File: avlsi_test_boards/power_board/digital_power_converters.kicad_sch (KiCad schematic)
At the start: 21 parts, among them U1 TLV1117LV18DCYR, U15 DS04-254-2-04BK-SMT, U20 74HC4051D_653, U3 TLV1117LV25DCYR, U4 TLV1117LV33DCYR

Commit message: Fully routed
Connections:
- net AVIN renamed VDCustom
- net GND renamed DGND
- net VIN renamed DVIN5

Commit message: Add partial changes
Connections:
- net NULL is gone; now on net DGND: U20.2 (Y6), U20.4 (Y7)
- net DGND: now also U15.5
- net VCCD12: now also U20.14 (Y1); no longer U20.15 (Y2)
- net VCCD18: now also U20.15 (Y2); no longer U20.14 (Y1)
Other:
- moved on the sheet: C18, R15, R16, R17

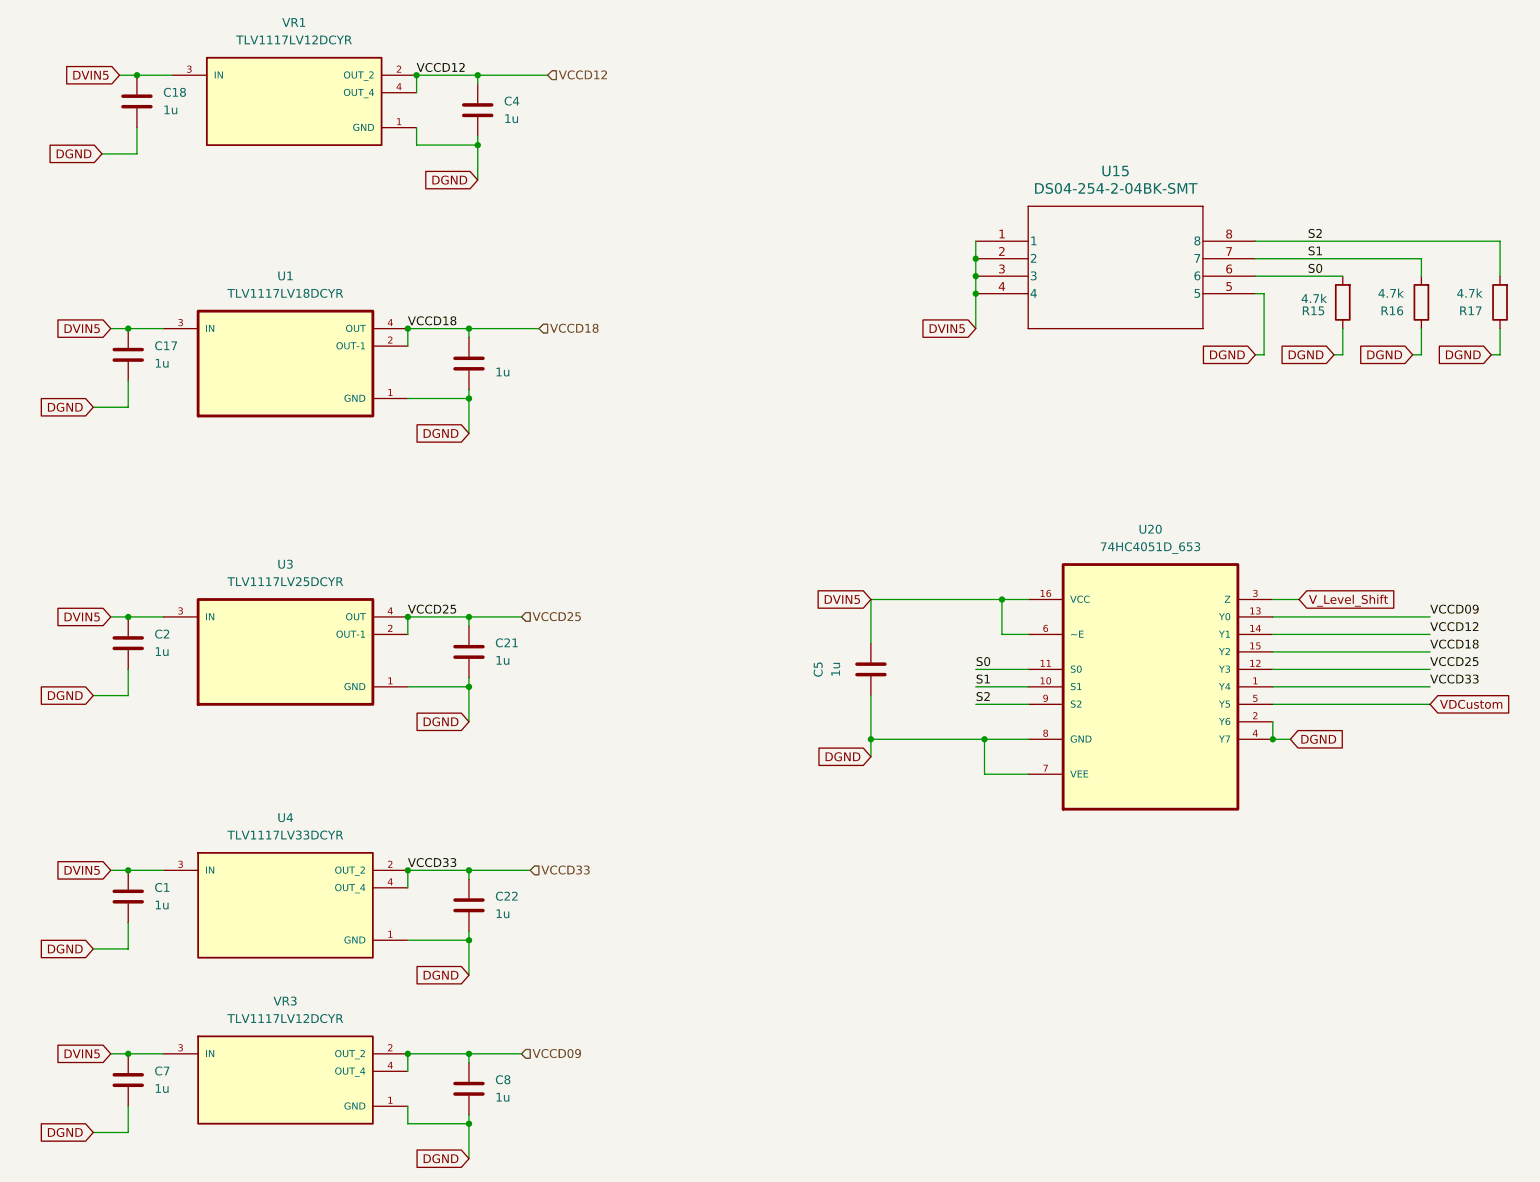
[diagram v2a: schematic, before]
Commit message: Add updated schematic
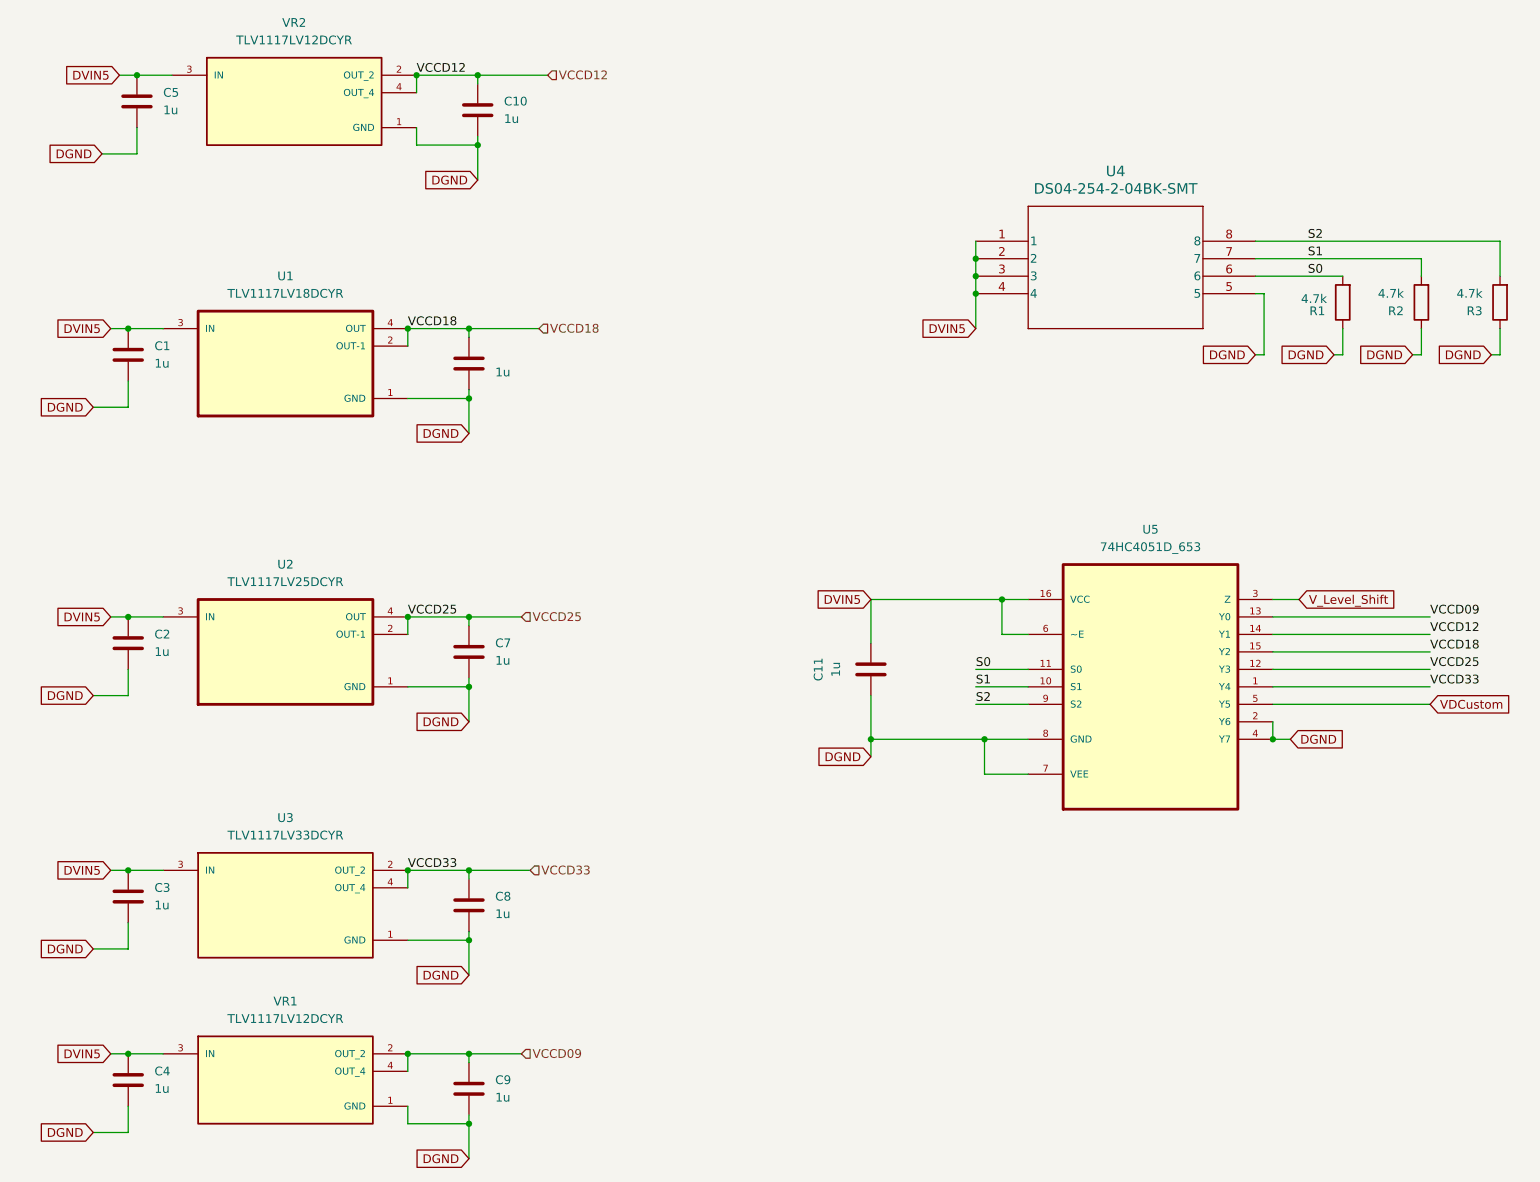
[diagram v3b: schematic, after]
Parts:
- renumbered C17 to C1, C4 to C10, C5 to C11, C1 to C3, C7 to C4, C18 to C5, C3 to C6, C21 to C7, C22 to C8, C8 to C9, R15 to R1, R16 to R2, R17 to R3, U3 to U2, U4 to U3, U15 to U4, U20 to U5, VR3 to VR1, VR1 to VR2
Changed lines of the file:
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@@
 		(dnp no)
 		(fields_autoplaced yes)
-		(property "Reference" "C18"
+		(property "Reference" "C5"
 			(at 64.77 40.6399 0)
 			(effects
@@
 			(project "power_board"
 				(path "/425e3f4e-d960-41c8-a4b7-4f888de39c97/572e1625-24a1-4783-bac1-8c305a89efd3"
-					(reference "C18")
+					(reference "C5")
 					(unit 1)
 				)
@@
 		(on_board yes)
 		(dnp no)
-		(property "Reference" "C5"
+		(property "Reference" "C11"
 			(at 160.02 124.46 90)
 			(effects
@@
 			(project "power_board"
 				(path "/425e3f4e-d960-41c8-a4b7-4f888de39c97/572e1625-24a1-4783-bac1-8c305a89efd3"
-					(reference "C5")
+					(reference "C11")
 					(unit 1)
 				)
@@
 		(dnp no)
 		(fields_autoplaced yes)
-		(property "Reference" "VR1"
+		(property "Reference" "VR2"
 			(at 83.82 30.48 0)
 			(effects
@@
 			(project "power_board"
 				(path "/425e3f4e-d960-41c8-a4b7-4f888de39c97/572e1625-24a1-4783-bac1-8c305a89efd3"
-					(reference "VR1")
+					(reference "VR2")
 					(unit 1)
 				)
@@
 		(dnp no)
 		(fields_autoplaced yes)
-		(property "Reference" "C21"
+		(property "Reference" "C7"
 			(at 113.03 120.6499 0)
 			(effects
@@
 			(project "power_board"
 				(path "/425e3f4e-d960-41c8-a4b7-4f888de39c97/572e1625-24a1-4783-bac1-8c305a89efd3"
-					(reference "C21")
+					(reference "C7")
 					(unit 1)
 				)
@@
 		(dnp no)
 		(fields_autoplaced yes)
-		(property "Reference" "C4"
+		(property "Reference" "C10"
 			(at 114.3 41.9099 0)
 			(effects
@@
 			(project "power_board"
 				(path "/425e3f4e-d960-41c8-a4b7-4f888de39c97/572e1625-24a1-4783-bac1-8c305a89efd3"
-					(reference "C4")
+					(reference "C10")
 					(unit 1)
 				)
@@
 		(dnp no)
 		(fields_autoplaced yes)
-		(property "Reference" "C7"
+		(property "Reference" "C4"
 			(at 63.5 182.8799 0)
 			(effects
@@
 			(project "power_board"
 				(path "/425e3f4e-d960-41c8-a4b7-4f888de39c97/572e1625-24a1-4783-bac1-8c305a89efd3"
-					(reference "C7")
+					(reference "C4")
 					(unit 1)
 				)
@@
 		(dnp no)
 		(fields_autoplaced yes)
-		(property "Reference" "VR3"
+		(property "Reference" "VR1"
 			(at 82.55 172.72 0)
 			(effects
@@
 			(project "power_board"
 				(path "/425e3f4e-d960-41c8-a4b7-4f888de39c97/572e1625-24a1-4783-bac1-8c305a89efd3"
-					(reference "VR3")
+					(reference "VR1")
 					(unit 1)
 				)
@@
 		(dnp no)
 		(fields_autoplaced yes)
-		(property "Reference" "U3"
+		(property "Reference" "U2"
 			(at 82.55 109.22 0)
 			(effects
@@
 			(project "power_board"
 				(path "/425e3f4e-d960-41c8-a4b7-4f888de39c97/572e1625-24a1-4783-bac1-8c305a89efd3"
-					(reference "U3")
+					(reference "U2")
 					(unit 1)
 				)
@@
 		(dnp no)
 		(fields_autoplaced yes)
-		(property "Reference" "C22"
+		(property "Reference" "C8"
 			(at 113.03 157.4799 0)
 			(effects
@@
 			(project "power_board"
 				(path "/425e3f4e-d960-41c8-a4b7-4f888de39c97/572e1625-24a1-4783-bac1-8c305a89efd3"
-					(reference "C22")
+					(reference "C8")
 					(unit 1)
 				)
@@
 		(dnp no)
 		(fields_autoplaced yes)
-		(property "Reference" "C8"
+		(property "Reference" "C9"
 			(at 113.03 184.1499 0)
 			(effects
@@
 			(project "power_board"
 				(path "/425e3f4e-d960-41c8-a4b7-4f888de39c97/572e1625-24a1-4783-bac1-8c305a89efd3"
-					(reference "C8")
+					(reference "C9")
 					(unit 1)
 				)
@@
 		(dnp no)
 		(fields_autoplaced yes)
-		(property "Reference" "C1"
+		(property "Reference" "C3"
 			(at 63.5 156.2099 0)
 			(effects
@@
 			(project "power_board"
 				(path "/425e3f4e-d960-41c8-a4b7-4f888de39c97/572e1625-24a1-4783-bac1-8c305a89efd3"
-					(reference "C1")
+					(reference "C3")
 					(unit 1)
 				)
@@
 		(dnp no)
 		(fields_autoplaced yes)
-		(property "Reference" "C3"
+		(property "Reference" "C6"
 			(at 113.03 78.7399 0)
 			(effects
@@
 			(project "power_board"
 				(path "/425e3f4e-d960-41c8-a4b7-4f888de39c97/572e1625-24a1-4783-bac1-8c305a89efd3"
-					(reference "C3")
+					(reference "C6")
 					(unit 1)
 				)
@@
 		(dnp no)
 		(fields_autoplaced yes)
-		(property "Reference" "R17"
+		(property "Reference" "R3"
 			(at 256.54 72.3901 0)
 			(effects
@@
 			(project "power_board"
 				(path "/425e3f4e-d960-41c8-a4b7-4f888de39c97/572e1625-24a1-4783-bac1-8c305a89efd3"
-					(reference "R17")
+					(reference "R3")
 					(unit 1)
 				)
@@
 		(dnp no)
 		(fields_autoplaced yes)
-		(property "Reference" "U20"
+		(property "Reference" "U5"
 			(at 208.28 104.14 0)
 			(effects
@@
 			(project "power_board"
 				(path "/425e3f4e-d960-41c8-a4b7-4f888de39c97/572e1625-24a1-4783-bac1-8c305a89efd3"
-					(reference "U20")
+					(reference "U5")
 					(unit 1)
 				)
@@
 		(dnp no)
 		(fields_autoplaced yes)
-		(property "Reference" "R16"
+		(property "Reference" "R2"
 			(at 245.11 72.3901 0)
 			(effects
@@
 			(project "power_board"
 				(path "/425e3f4e-d960-41c8-a4b7-4f888de39c97/572e1625-24a1-4783-bac1-8c305a89efd3"
-					(reference "R16")
+					(reference "R2")
 					(unit 1)
 				)
@@
 		(dnp no)
 		(fields_autoplaced yes)
-		(property "Reference" "U15"
+		(property "Reference" "U4"
 			(at 203.2 52.07 0)
 			(effects
@@
 			(project "power_board"
 				(path "/425e3f4e-d960-41c8-a4b7-4f888de39c97/572e1625-24a1-4783-bac1-8c305a89efd3"
-					(reference "U15")
+					(reference "U4")
 					(unit 1)
 				)
@@
 		(dnp no)
 		(fields_autoplaced yes)
-		(property "Reference" "C17"
+		(property "Reference" "C1"
 			(at 63.5 77.4699 0)
 			(effects
@@
 			(project "power_board"
 				(path "/425e3f4e-d960-41c8-a4b7-4f888de39c97/572e1625-24a1-4783-bac1-8c305a89efd3"
-					(reference "C17")
+					(reference "C1")
 					(unit 1)
 				)
@@
 		(on_board yes)
 		(dnp no)
-		(property "Reference" "U4"
+		(property "Reference" "U3"
 			(at 82.55 146.05 0)
 			(effects
@@
 			(project "power_board"
 				(path "/425e3f4e-d960-41c8-a4b7-4f888de39c97/572e1625-24a1-4783-bac1-8c305a89efd3"
-					(reference "U4")
+					(reference "U3")
 					(unit 1)
 				)
@@
 		(on_board yes)
 		(dnp no)
-		(property "Reference" "R15"
+		(property "Reference" "R1"
 			(at 233.68 72.3901 0)
 			(effects
@@
 			(project "power_board"
 				(path "/425e3f4e-d960-41c8-a4b7-4f888de39c97/572e1625-24a1-4783-bac1-8c305a89efd3"
-					(reference "R15")
-					(unit 1)
-				)
+					(reference "R1")
+					(unit 1)
+				)

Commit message: Add initial layout stuff
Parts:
- C1, C10, C11, C2, C3, C4, C5, C6, C7, C8, C9: footprint Capacitor_SMD:C_0603_1608Metric -> Capacitor_SMD:C_0805_2012Metric
- R1, R2, R3: footprint Resistor_SMD:R_0201_0603Metric -> Resistor_SMD:R_0805_2012Metric
- U4: footprint DS04-254-2-04BK-SMT_CUD -> ds:DS04-254-2-04BK-SMT_CUD
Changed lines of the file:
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@@
 			)
 		)
-		(property "Footprint" "Capacitor_SMD:C_0603_1608Metric"
+		(property "Footprint" "Capacitor_SMD:C_0805_2012Metric"
 			(at 61.9252 45.72 0)
 			(effects
@@
 			)
 		)
-		(property "Footprint" "Capacitor_SMD:C_0603_1608Metric"
+		(property "Footprint" "Capacitor_SMD:C_0805_2012Metric"
 			(at 168.6052 120.65 0)
 			(effects
@@
 			)
 		)
-		(property "Footprint" "Capacitor_SMD:C_0603_1608Metric"
+		(property "Footprint" "Capacitor_SMD:C_0805_2012Metric"
 			(at 110.1852 125.73 0)
 			(effects
@@
 			)
 		)
-		(property "Footprint" "Capacitor_SMD:C_0603_1608Metric"
+		(property "Footprint" "Capacitor_SMD:C_0805_2012Metric"
 			(at 111.4552 46.99 0)
 			(effects
@@
 			)
 		)
-		(property "Footprint" "Capacitor_SMD:C_0603_1608Metric"
+		(property "Footprint" "Capacitor_SMD:C_0805_2012Metric"
 			(at 60.6552 187.96 0)
 			(effects
@@
 			)
 		)
-		(property "Footprint" "Capacitor_SMD:C_0603_1608Metric"
+		(property "Footprint" "Capacitor_SMD:C_0805_2012Metric"
 			(at 60.6552 124.46 0)
 			(effects
@@
 			)
 		)
-		(property "Footprint" "Capacitor_SMD:C_0603_1608Metric"
+		(property "Footprint" "Capacitor_SMD:C_0805_2012Metric"
 			(at 110.1852 162.56 0)
 			(effects
@@
 			)
 		)
-		(property "Footprint" "Capacitor_SMD:C_0603_1608Metric"
+		(property "Footprint" "Capacitor_SMD:C_0805_2012Metric"
 			(at 110.1852 189.23 0)
 			(effects
@@
 			)
 		)
-		(property "Footprint" "Capacitor_SMD:C_0603_1608Metric"
+		(property "Footprint" "Capacitor_SMD:C_0805_2012Metric"
 			(at 60.6552 161.29 0)
 			(effects
@@
 			)
 		)
-		(property "Footprint" "Capacitor_SMD:C_0603_1608Metric"
+		(property "Footprint" "Capacitor_SMD:C_0805_2012Metric"
 			(at 110.1852 83.82 0)
 			(effects
@@
 			)
 		)
-		(property "Footprint" "Resistor_SMD:R_0201_0603Metric"
+		(property "Footprint" "Resistor_SMD:R_0805_2012Metric"
 			(at 260.858 71.12 90)
 			(effects
@@
 			)
 		)
-		(property "Footprint" "Resistor_SMD:R_0201_0603Metric"
+		(property "Footprint" "Resistor_SMD:R_0805_2012Metric"
 			(at 249.428 71.12 90)
 			(effects
@@
 			)
 		)
-		(property "Footprint" "DS04-254-2-04BK-SMT_CUD"
+		(property "Footprint" "ds:DS04-254-2-04BK-SMT_CUD"
 			(at 182.88 62.23 0)
 			(effects
@@
 			)
 		)
-		(property "Footprint" "Capacitor_SMD:C_0603_1608Metric"
+		(property "Footprint" "Capacitor_SMD:C_0805_2012Metric"
 			(at 60.6552 82.55 0)
 			(effects
@@
 			)
 		)
-		(property "Footprint" "Resistor_SMD:R_0201_0603Metric"
+		(property "Footprint" "Resistor_SMD:R_0805_2012Metric"
 			(at 237.998 71.12 90)
 			(effects
